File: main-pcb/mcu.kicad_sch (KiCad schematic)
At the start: 74 parts, among them J11 CONN_01X03, J12 PMOD_HOST, J13 PMOD_HOST, J4 CORTEX_DEBUG_ETM, J5 CONN_01X03, U1 XC7S100-1FGGA484C, U12 AT24MAC402, U13 ECS-1612MV-250-CN, U14 STM32H735-UFBGA176-25, U15 S27KL0642GABHB020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

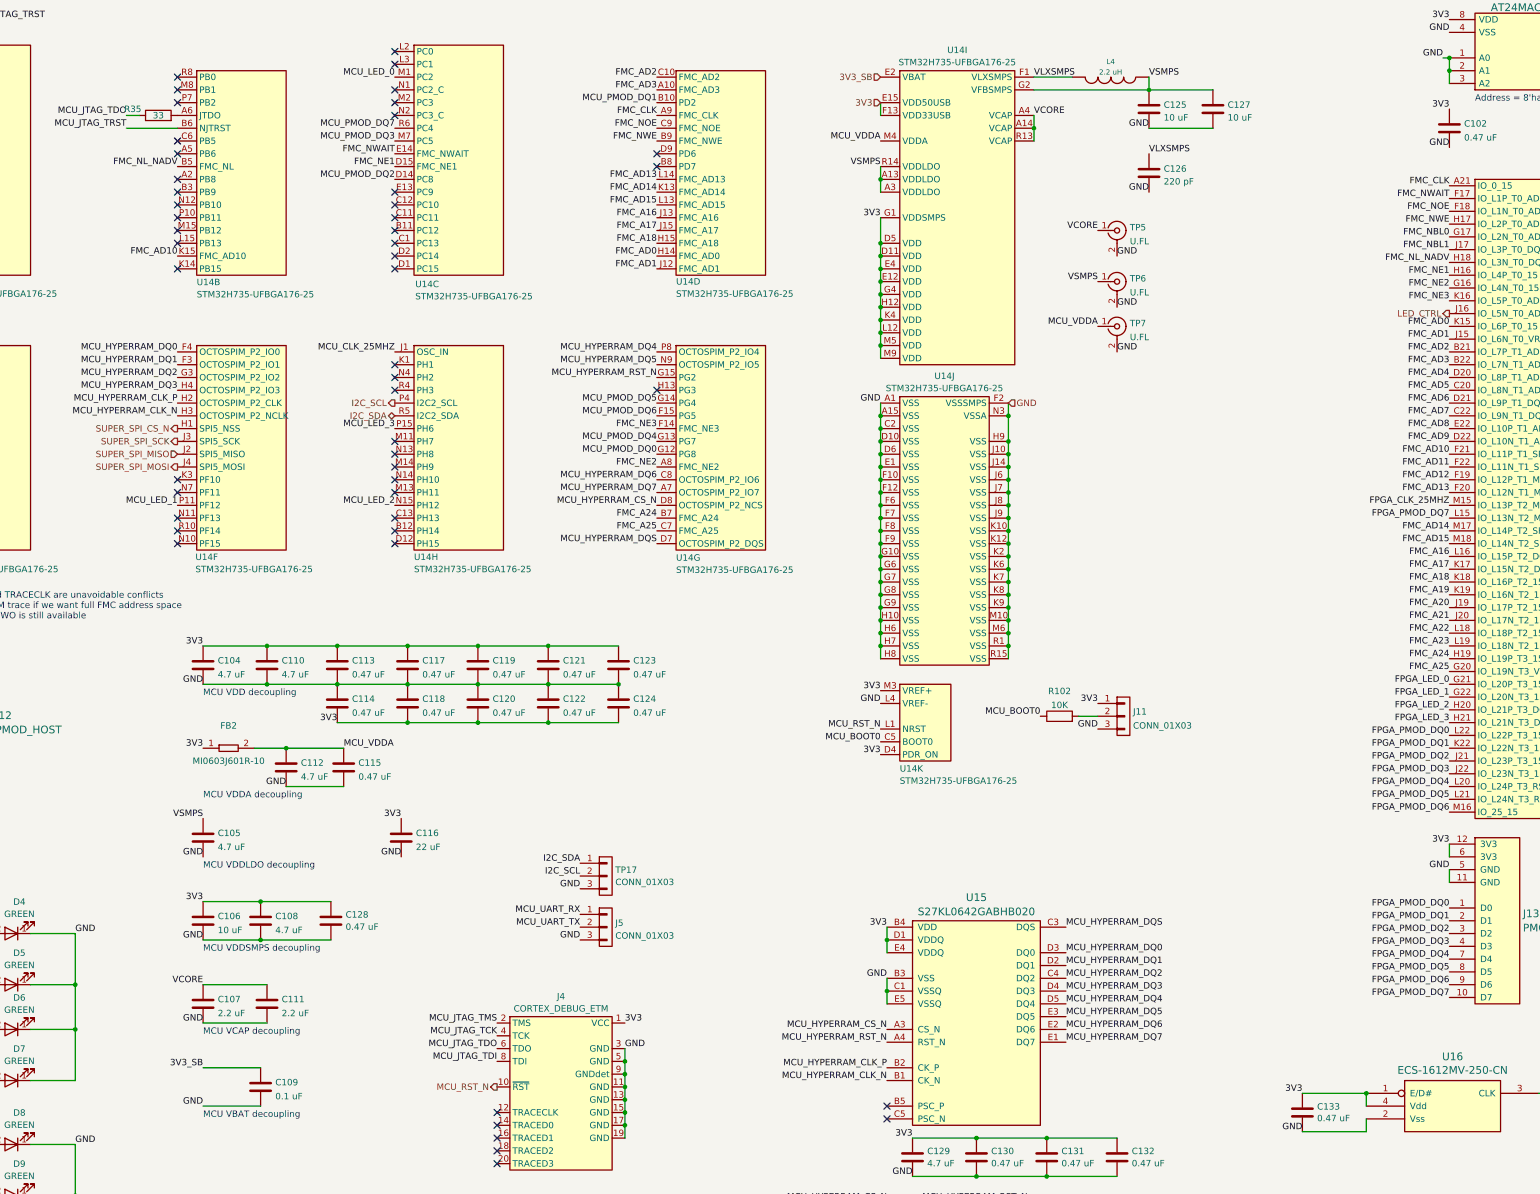
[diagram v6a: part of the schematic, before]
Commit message: Started work on main CPU routing
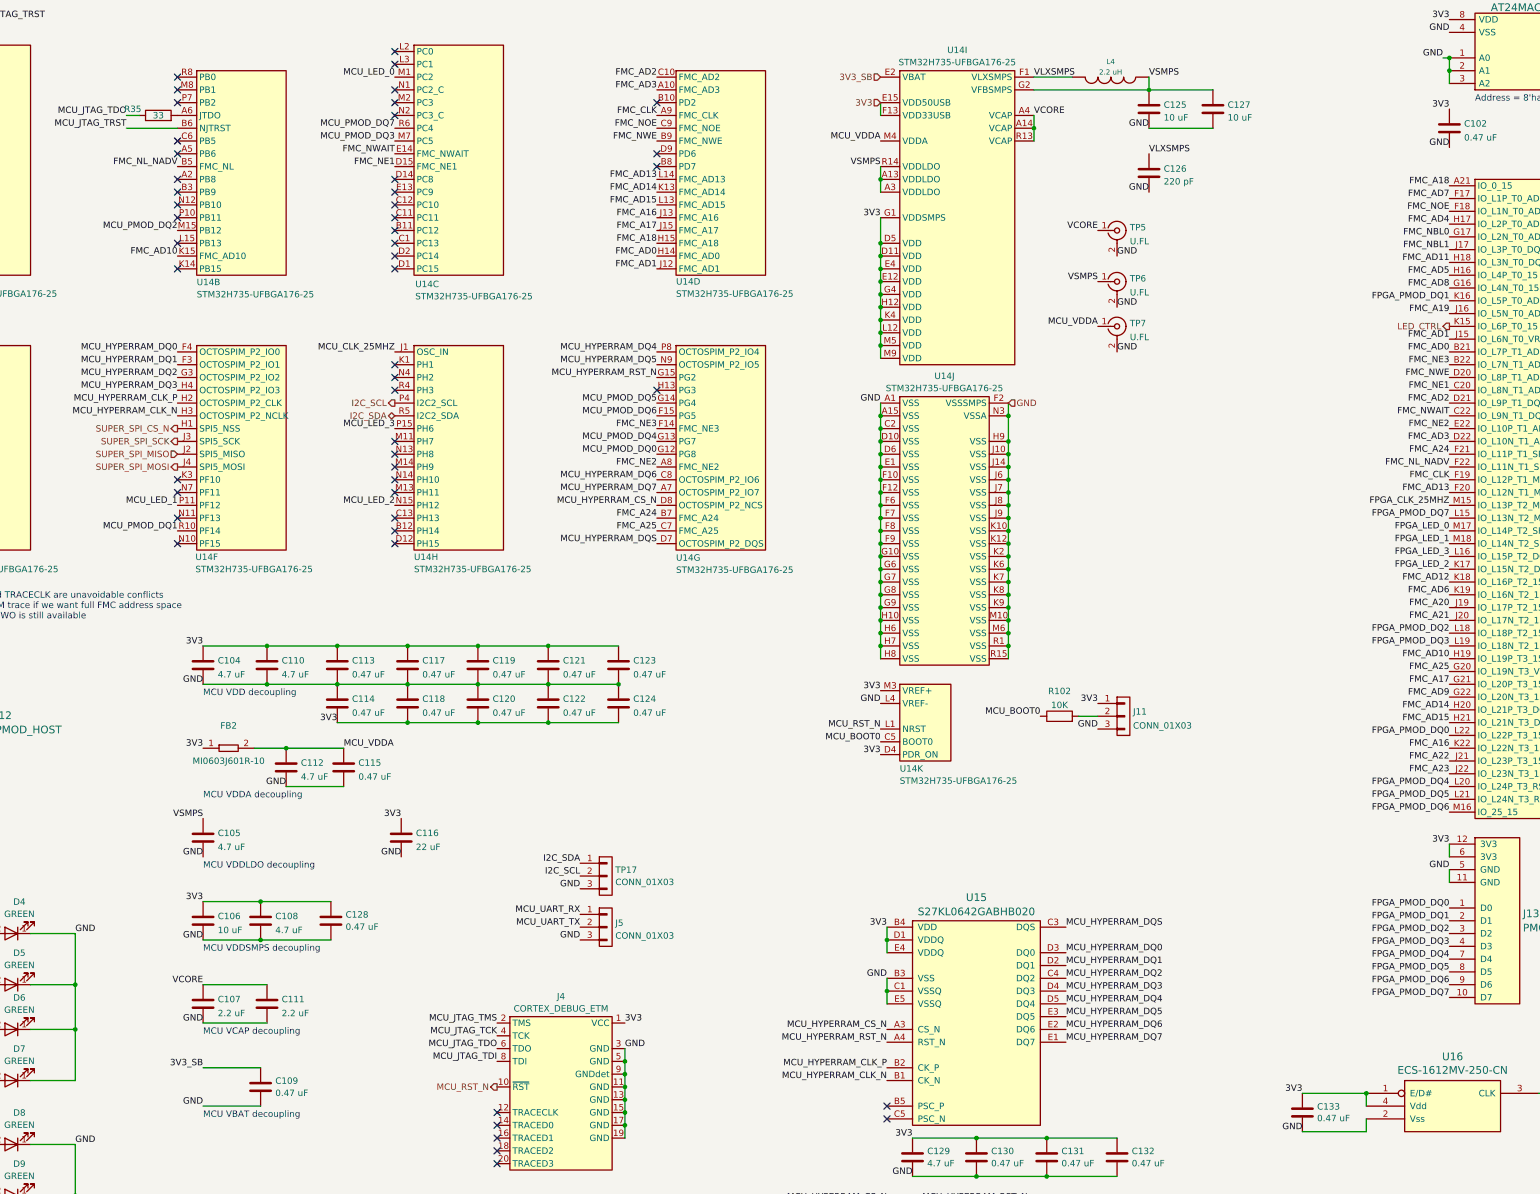
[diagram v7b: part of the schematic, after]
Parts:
- C109: value 0.1 uF -> 0.47 uF
- C128: footprint azonenberg_pcb:EIA_0603_CAP_NOSILK -> azonenberg_pcb:EIA_0402_CAP_NOSILK
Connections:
- net FMC_A16: now also U1.K22 (IO_L22N_T3_15); no longer U1.L16 (IO_L15P_T2_DQS_15)
- net FMC_A17: now also U1.G21 (IO_L20P_T3_15); no longer U1.K17 (IO_L15N_T2_DQS_15)
- net FMC_A18: now also U1.A21 (IO_0_15); no longer U1.K18 (IO_L16P_T2_15)
- net FMC_A19: now also U1.J16 (IO_L5N_T0_AD9N_15); no longer U1.K19 (IO_L16N_T2_15)
- net FMC_A22: now also U1.J21 (IO_L23P_T3_15); no longer U1.L18 (IO_L18P_T2_15)
- net FMC_A23: now also U1.J22 (IO_L23N_T3_15); no longer U1.L19 (IO_L18N_T2_15)
- net FMC_A24: now also U1.F21 (IO_L11P_T1_SRCC_15); no longer U1.H19 (IO_L19P_T3_15)
- net FMC_AD0: now also U1.B21 (IO_L7P_T1_AD2P_15); no longer U1.K15 (IO_L6P_T0_15)
- net FMC_AD10: now also U1.H19 (IO_L19P_T3_15); no longer U1.F21 (IO_L11P_T1_SRCC_15)
- net FMC_AD11: now also U1.H18 (IO_L3N_T0_DQS_AD1N_15); no longer U1.F22 (IO_L11N_T1_SRCC_15)
- net FMC_AD12: now also U1.K18 (IO_L16P_T2_15); no longer U1.F19 (IO_L12P_T1_MRCC_15)
- net FMC_AD14: now also U1.H20 (IO_L21P_T3_DQS_15); no longer U1.M17 (IO_L14P_T2_SRCC_15)
- net FMC_AD15: now also U1.H21 (IO_L21N_T3_DQS_15); no longer U1.M18 (IO_L14N_T2_SRCC_15)
- net FMC_AD2: now also U1.D21 (IO_L9P_T1_DQS_AD3P_15); no longer U1.B21 (IO_L7P_T1_AD2P_15)
- net FMC_AD3: now also U1.D22 (IO_L10N_T1_AD11N_15); no longer U1.B22 (IO_L7N_T1_AD2N_15)
- net FMC_AD4: now also U1.H17 (IO_L2P_T0_AD8P_15); no longer U1.D20 (IO_L8P_T1_AD10P_15)
- net FMC_AD5: now also U1.H16 (IO_L4P_T0_15); no longer U1.C20 (IO_L8N_T1_AD10N_15)
- net FMC_AD6: now also U1.K19 (IO_L16N_T2_15); no longer U1.D21 (IO_L9P_T1_DQS_AD3P_15)
- net FMC_AD7: now also U1.F17 (IO_L1P_T0_AD0P_15); no longer U1.C22 (IO_L9N_T1_DQS_AD3N_15)
- net FMC_AD8: now also U1.G16 (IO_L4N_T0_15); no longer U1.E22 (IO_L10P_T1_AD11P_15)
- net FMC_AD9: now also U1.G22 (IO_L20N_T3_15); no longer U1.D22 (IO_L10N_T1_AD11N_15)
- net FMC_CLK: now also U1.F19 (IO_L12P_T1_MRCC_15); no longer U1.A21 (IO_0_15)
- net FMC_NE1: now also U1.C20 (IO_L8N_T1_AD10N_15); no longer U1.H16 (IO_L4P_T0_15)
- net FMC_NE2: now also U1.E22 (IO_L10P_T1_AD11P_15); no longer U1.G16 (IO_L4N_T0_15)
- net FMC_NE3: now also U1.B22 (IO_L7N_T1_AD2N_15); no longer U1.K16 (IO_L5P_T0_AD9P_15)
- net FMC_NL_NADV: now also U1.F22 (IO_L11N_T1_SRCC_15); no longer U1.H18 (IO_L3N_T0_DQS_AD1N_15)
- net FMC_NWAIT: now also U1.C22 (IO_L9N_T1_DQS_AD3N_15); no longer U1.F17 (IO_L1P_T0_AD0P_15)
- net FMC_NWE: now also U1.D20 (IO_L8P_T1_AD10P_15); no longer U1.H17 (IO_L2P_T0_AD8P_15)
- net FPGA_LED_0: now also U1.M17 (IO_L14P_T2_SRCC_15); no longer U1.G21 (IO_L20P_T3_15)
- net FPGA_LED_1: now also U1.M18 (IO_L14N_T2_SRCC_15); no longer U1.G22 (IO_L20N_T3_15)
- net FPGA_LED_2: now also U1.K17 (IO_L15N_T2_DQS_15); no longer U1.H20 (IO_L21P_T3_DQS_15)
- net FPGA_LED_3: now also U1.L16 (IO_L15P_T2_DQS_15); no longer U1.H21 (IO_L21N_T3_DQS_15)
- net FPGA_PMOD_DQ1: now also U1.K16 (IO_L5P_T0_AD9P_15); no longer U1.K22 (IO_L22N_T3_15)
- net FPGA_PMOD_DQ2: now also U1.L18 (IO_L18P_T2_15); no longer U1.J21 (IO_L23P_T3_15)
- net FPGA_PMOD_DQ3: now also U1.L19 (IO_L18N_T2_15); no longer U1.J22 (IO_L23N_T3_15)
- net LED_CTRL: now also U1.K15 (IO_L6P_T0_15); no longer U1.J16 (IO_L5N_T0_AD9N_15)
- net MCU_PMOD_DQ1: now also U14.R10 (PF14); no longer U14.B10 (PD2)
- net MCU_PMOD_DQ2: now also U14.M15 (PB12); no longer U14.D14 (PC8)
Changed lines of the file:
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@@
 	)
 	(no_connect
+		(at 143.51 52.07)
+	)
+	(no_connect
 		(at 163.83 240.03)
 	)
@@
 	)
 	(no_connect
-		(at 100.33 62.23)
-	)
-	(no_connect
 		(at 195.58 46.99)
 	)
 	(no_connect
-		(at 100.33 121.92)
-	)
-	(no_connect
 		(at 100.33 119.38)
 	)
@@
 	)
 	(no_connect
+		(at 195.58 36.83)
+	)
+	(no_connect
 		(at 100.33 59.69)
 	)
@@
 	)
 	(label "FMC_A23"
-		(at 353.06 144.78 180)
+		(at 353.06 170.18 180)
 		(fields_autoplaced yes)
 		(effects
@@
 	)
 	(label "MCU_PMOD_DQ2"
-		(at 143.51 52.07 180)
+		(at 100.33 62.23 180)
 		(fields_autoplaced yes)
 		(effects
@@
 	)
 	(label "FMC_AD3"
-		(at 353.06 88.9 180)
+		(at 353.06 104.14 180)
 		(fields_autoplaced yes)
 		(effects
@@
 	)
 	(label "FMC_A19"
-		(at 353.06 134.62 180)
+		(at 353.06 78.74 180)
 		(fields_autoplaced yes)
 		(effects
@@
 	)
 	(label "FMC_NE1"
-		(at 353.06 71.12 180)
+		(at 353.06 93.98 180)
 		(fields_autoplaced yes)
 		(effects
@@
 	)
 	(label "FMC_AD10"
-		(at 353.06 106.68 180)
+		(at 353.06 147.32 180)
 		(fields_autoplaced yes)
 		(effects
@@
 	)
 	(label "FPGA_PMOD_DQ1"
-		(at 353.06 165.1 180)
+		(at 353.06 76.2 180)
 		(fields_autoplaced yes)
 		(effects
@@
 	)
 	(label "MCU_PMOD_DQ1"
-		(at 195.58 36.83 180)
+		(at 100.33 121.92 180)
 		(fields_autoplaced yes)
 		(effects
@@
 	)
 	(label "FMC_A18"
-		(at 353.06 132.08 180)
+		(at 353.06 53.34 180)
 		(fields_autoplaced yes)
 		(effects
@@
 	)
 	(label "FPGA_LED_0"
-		(at 353.06 152.4 180)
+		(at 353.06 121.92 180)
 		(fields_autoplaced yes)
 		(effects
@@
 	)
 	(label "FPGA_PMOD_DQ2"
-		(at 353.06 167.64 180)
+		(at 353.06 142.24 180)
 		(fields_autoplaced yes)
 		(effects
@@
 	)
 	(label "FPGA_LED_3"
-		(at 353.06 160.02 180)
+		(at 353.06 127 180)
 		(fields_autoplaced yes)
 		(effects
@@
 	)
 	(label "FMC_A16"
-		(at 353.06 127 180)
+		(at 353.06 165.1 180)
 		(fields_autoplaced yes)
 		(effects
@@
 	)
 	(label "FMC_A17"
-		(at 353.06 129.54 180)
+		(at 353.06 152.4 180)
 		(fields_autoplaced yes)
 		(effects
@@
 	)
 	(label "FMC_NE2"
-		(at 353.06 73.66 180)
+		(at 353.06 101.6 180)
 		(fields_autoplaced yes)
 		(effects
@@
 	)
 	(label "FMC_NL_NADV"
-		(at 353.06 68.58 180)
+		(at 353.06 109.22 180)
 		(fields_autoplaced yes)
 		(effects
@@
 	)
 	(label "FMC_CLK"
-		(at 353.06 53.34 180)
+		(at 353.06 111.76 180)
 		(fields_autoplaced yes)
 		(effects
@@
 	)
 	(label "FMC_NWE"
-		(at 353.06 60.96 180)
+		(at 353.06 91.44 180)
 		(fields_autoplaced yes)
 		(effects
@@
 	)
 	(label "FMC_A24"
-		(at 353.06 147.32 180)
+		(at 353.06 106.68 180)
 		(fields_autoplaced yes)
 		(effects
@@
 	)
 	(label "FMC_NWAIT"
-		(at 353.06 55.88 180)
+		(at 353.06 99.06 180)
 		(fields_autoplaced yes)
 		(effects
@@
 	)
 	(label "FMC_NE3"
-		(at 353.06 76.2 180)
+		(at 353.06 88.9 180)
 		(fields_autoplaced yes)
 		(effects
@@
 	)
 	(label "FPGA_LED_2"
-		(at 353.06 157.48 180)
+		(at 353.06 129.54 180)
 		(fields_autoplaced yes)
 		(effects
@@
 	)
 	(label "FMC_AD15"
-		(at 353.06 124.46 180)
+		(at 353.06 160.02 180)
 		(fields_autoplaced yes)
 		(effects
@@
 	)
 	(label "FMC_AD11"
-		(at 353.06 109.22 180)
+		(at 353.06 68.58 180)
 		(fields_autoplaced yes)
 		(effects
@@
 	)
 	(label "FMC_AD7"
-		(at 353.06 99.06 180)
+		(at 353.06 55.88 180)
 		(fields_autoplaced yes)
 		(effects
@@
 	)
 	(label "FMC_AD6"
-		(at 353.06 96.52 180)
+		(at 353.06 134.62 180)
 		(fields_autoplaced yes)
 		(effects
@@
 	)
 	(label "FMC_AD12"
-		(at 353.06 111.76 180)
+		(at 353.06 132.08 180)
 		(fields_autoplaced yes)
 		(effects
@@
 	)
 	(label "FMC_AD9"
-		(at 353.06 104.14 180)
+		(at 353.06 154.94 180)
 		(fields_autoplaced yes)
 		(effects
@@
 	)
 	(label "FMC_AD0"
-		(at 353.06 81.28 180)
+		(at 353.06 86.36 180)
 		(fields_autoplaced yes)
 		(effects
@@
 	)
 	(label "FMC_A22"
-		(at 353.06 142.24 180)
+		(at 353.06 167.64 180)
 		(fields_autoplaced yes)
 		(effects
@@
 	)
 	(label "FMC_AD14"
-		(at 353.06 121.92 180)
+		(at 353.06 157.48 180)
 		(fields_autoplaced yes)
 		(effects
@@
 	)
 	(label "FPGA_LED_1"
-		(at 353.06 154.94 180)
+		(at 353.06 124.46 180)
 		(fields_autoplaced yes)
 		(effects
@@
 	)
 	(label "FPGA_PMOD_DQ3"
-		(at 353.06 170.18 180)
+		(at 353.06 144.78 180)
 		(fields_autoplaced yes)
 		(effects
@@
 	)
 	(label "FMC_AD8"
-		(at 353.06 101.6 180)
+		(at 353.06 73.66 180)
 		(fields_autoplaced yes)
 		(effects
@@
 	)
 	(label "FMC_AD5"
-		(at 353.06 93.98 180)
+		(at 353.06 71.12 180)
 		(fields_autoplaced yes)
 		(effects
@@
 	)
 	(label "FMC_AD4"
-		(at 353.06 91.44 180)
+		(at 353.06 60.96 180)
 		(fields_autoplaced yes)
 		(effects
@@
 	)
 	(label "FMC_AD2"
-		(at 353.06 86.36 180)
+		(at 353.06 96.52 180)
 		(fields_autoplaced yes)
 		(effects
@@
 	(hierarchical_label "LED_CTRL"
 		(shape output)
-		(at 353.06 78.74 180)
+		(at 353.06 81.28 180)
 		(fields_autoplaced yes)
 		(effects
@@
 			)
 		)
-		(property "Footprint" "azonenberg_pcb:EIA_0603_CAP_NOSILK"
+		(property "Footprint" "azonenberg_pcb:EIA_0402_CAP_NOSILK"
 			(at 131.7752 203.2 0)
 			(effects
@@
 		(fields_autoplaced yes)
 		(property "Reference" "C109"
-			(at 119.761 231.5015 0)
+			(at 119.761 231.1978 0)
 			(effects
 				(font
@@
 			)
 		)
-		(property "Value" "0.1 uF"
-			(at 119.761 234.2766 0)
+		(property "Value" "0.47 uF"
+			(at 119.761 233.6221 0)
 			(effects
 				(font

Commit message: Continued routing MCU, started work on PHY
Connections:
- net FMC_A17: now also U1.G17 (IO_L2N_T0_AD8N_15); no longer U1.G21 (IO_L20P_T3_15)
- net FMC_A19: now also U1.H21 (IO_L21N_T3_DQS_15); no longer U1.J16 (IO_L5N_T0_AD9N_15)
- net FMC_A20: now also U1.J21 (IO_L23P_T3_15); no longer U1.J19 (IO_L17P_T2_15)
- net FMC_A21: now also U1.J22 (IO_L23N_T3_15); no longer U1.J20 (IO_L17N_T2_15)
- net FMC_A22: now also U1.J19 (IO_L17P_T2_15); no longer U1.J21 (IO_L23P_T3_15)
- net FMC_A23: now also U1.G22 (IO_L20N_T3_15); no longer U1.J22 (IO_L23N_T3_15)
- net FMC_A25: now also U1.J16 (IO_L5N_T0_AD9N_15); no longer U1.G20 (IO_L19N_T3_VREF_15)
- net FMC_AD10: now also U1.F20 (IO_L12N_T1_MRCC_15); no longer U1.H19 (IO_L19P_T3_15)
- net FMC_AD11: now also U1.F17 (IO_L1P_T0_AD0P_15); no longer U1.H18 (IO_L3N_T0_DQS_AD1N_15)
- net FMC_AD13: now also U1.G20 (IO_L19N_T3_VREF_15); no longer U1.F20 (IO_L12N_T1_MRCC_15)
- net FMC_AD14: now also U1.F18 (IO_L1N_T0_AD0N_15); no longer U1.H20 (IO_L21P_T3_DQS_15)
- net FMC_AD15: now also U1.H19 (IO_L19P_T3_15); no longer U1.H21 (IO_L21N_T3_DQS_15)
- net FMC_AD7: now also U1.H18 (IO_L3N_T0_DQS_AD1N_15); no longer U1.F17 (IO_L1P_T0_AD0P_15)
- net FMC_AD9: now also U1.J20 (IO_L17N_T2_15); no longer U1.G22 (IO_L20N_T3_15)
- net FMC_NBL0: now also U1.G21 (IO_L20P_T3_15); no longer U1.G17 (IO_L2N_T0_AD8N_15)
- net FMC_NOE: now also U1.H20 (IO_L21P_T3_DQS_15); no longer U1.F18 (IO_L1N_T0_AD0N_15)
- net MCU_HYPERRAM_RST_N: now also U14.R7 (PA6); no longer U14.G15 (PG2)
- net MCU_PMOD_DQ0: now also U14.P10 (PB11); no longer U14.G12 (PG8)
- net MCU_PMOD_DQ4: now also U14.P12 (PE12); no longer U14.G13 (PG7)
- net MCU_PMOD_DQ5: now also U14.P13 (PE13); no longer U14.G14 (PG4)
- net MCU_PMOD_DQ6: now also U14.R8 (PB0); no longer U14.F15 (PG5)
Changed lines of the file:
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@@
 	(title_block
 		(title "DUMPTRUCK flash dumper")
-		(date "2024-10-19")
+		(date "2024-10-20")
 		(rev "0.1")
 		(company "Antikernel Labs")
@@
 	)
 	(no_connect
-		(at 49.53 119.38)
+		(at 195.58 91.44)
 	)
 	(no_connect
@@
 	)
 	(no_connect
-		(at 49.53 46.99)
-	)
-	(no_connect
-		(at 100.33 31.75)
+		(at 195.58 106.68)
 	)
 	(no_connect
@@
 	)
 	(no_connect
-		(at 143.51 121.92)
+		(at 100.33 57.15)
 	)
 	(no_connect
-		(at 100.33 114.3)
+		(at 143.51 121.92)
 	)
 	(no_connect
-		(at 100.33 57.15)
+		(at 100.33 114.3)
 	)
 	(no_connect
@@
 	)
 	(no_connect
+		(at 195.58 104.14)
+	)
+	(no_connect
 		(at 100.33 52.07)
 	)
@@
 	)
 	(no_connect
+		(at 195.58 99.06)
+	)
+	(no_connect
 		(at 49.53 34.29)
 	)
@@
 	)
 	(no_connect
+		(at 195.58 96.52)
+	)
+	(no_connect
 		(at 100.33 119.38)
 	)
@@
 	)
 	(no_connect
-		(at 100.33 59.69)
-	)
-	(no_connect
 		(at 143.51 114.3)
 	)
@@
 	)
 	(no_connect
-		(at 49.53 116.84)
-	)
-	(no_connect
 		(at 143.51 64.77)
 	)
@@
 	)
 	(label "FMC_A23"
-		(at 353.06 170.18 180)
+		(at 353.06 154.94 180)
 		(fields_autoplaced yes)
 		(effects
@@
 	)
 	(label "FMC_A20"
-		(at 353.06 137.16 180)
+		(at 353.06 167.64 180)
 		(fields_autoplaced yes)
 		(effects
@@
 	)
 	(label "FMC_A19"
-		(at 353.06 78.74 180)
+		(at 353.06 160.02 180)
 		(fields_autoplaced yes)
 		(effects
@@
 	)
 	(label "MCU_PMOD_DQ4"
-		(at 195.58 104.14 180)
+		(at 49.53 116.84 180)
 		(fields_autoplaced yes)
 		(effects
@@
 	)
 	(label "FMC_AD10"
-		(at 353.06 147.32 180)
+		(at 353.06 114.3 180)
 		(fields_autoplaced yes)
 		(effects
@@
 	)
 	(label "MCU_PMOD_DQ5"
-		(at 195.58 96.52 180)
+		(at 49.53 119.38 180)
 		(fields_autoplaced yes)
 		(effects
@@
 	)
 	(label "FMC_A17"
-		(at 353.06 152.4 180)
+		(at 353.06 63.5 180)
 		(fields_autoplaced yes)
 		(effects
@@
 	)
 	(label "FMC_NBL0"
-		(at 353.06 63.5 180)
+		(at 353.06 152.4 180)
 		(fields_autoplaced yes)
 		(effects
@@
 	)
 	(label "MCU_PMOD_DQ6"
-		(at 195.58 99.06 180)
+		(at 100.33 31.75 180)
 		(fields_autoplaced yes)
 		(effects
@@
 	)
 	(label "FMC_NOE"
-		(at 353.06 58.42 180)
+		(at 353.06 157.48 180)
 		(fields_autoplaced yes)
 		(effects
@@
 	)
 	(label "FMC_AD13"
-		(at 353.06 114.3 180)
+		(at 353.06 149.86 180)
 		(fields_autoplaced yes)
 		(effects
@@
 	)
 	(label "MCU_HYPERRAM_RST_N"
-		(at 195.58 91.44 180)
+		(at 49.53 46.99 180)
 		(fields_autoplaced yes)
 		(effects
@@
 	)
 	(label "MCU_PMOD_DQ0"
-		(at 195.58 106.68 180)
+		(at 100.33 59.69 180)
 		(fields_autoplaced yes)
 		(effects
@@
 	)
 	(label "FMC_A25"
-		(at 353.06 149.86 180)
+		(at 353.06 78.74 180)
 		(fields_autoplaced yes)
 		(effects
@@
 	)
 	(label "FMC_AD15"
-		(at 353.06 160.02 180)
+		(at 353.06 147.32 180)
 		(fields_autoplaced yes)
 		(effects
@@
 	)
 	(label "FMC_AD11"
-		(at 353.06 68.58 180)
+		(at 353.06 55.88 180)
 		(fields_autoplaced yes)
 		(effects
@@
 	)
 	(label "FMC_AD7"
-		(at 353.06 55.88 180)
+		(at 353.06 68.58 180)
 		(fields_autoplaced yes)
 		(effects
@@
 	)
 	(label "FMC_AD9"
-		(at 353.06 154.94 180)
+		(at 353.06 139.7 180)
 		(fields_autoplaced yes)
 		(effects
@@
 	)
 	(label "FMC_A22"
-		(at 353.06 167.64 180)
+		(at 353.06 137.16 180)
 		(fields_autoplaced yes)
 		(effects
@@
 	)
 	(label "FMC_AD14"
-		(at 353.06 157.48 180)
+		(at 353.06 58.42 180)
 		(fields_autoplaced yes)
 		(effects
@@
 	)
 	(label "FMC_A21"
-		(at 353.06 139.7 180)
+		(at 353.06 170.18 180)
 		(fields_autoplaced yes)
 		(effects
@@
 		(on_board yes)
 		(dnp no)
-		(fields_autoplaced yes)
 		(property "Reference" "U1"
 			(at 384.175 115.1008 0)
